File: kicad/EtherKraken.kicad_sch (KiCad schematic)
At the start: 4 parts

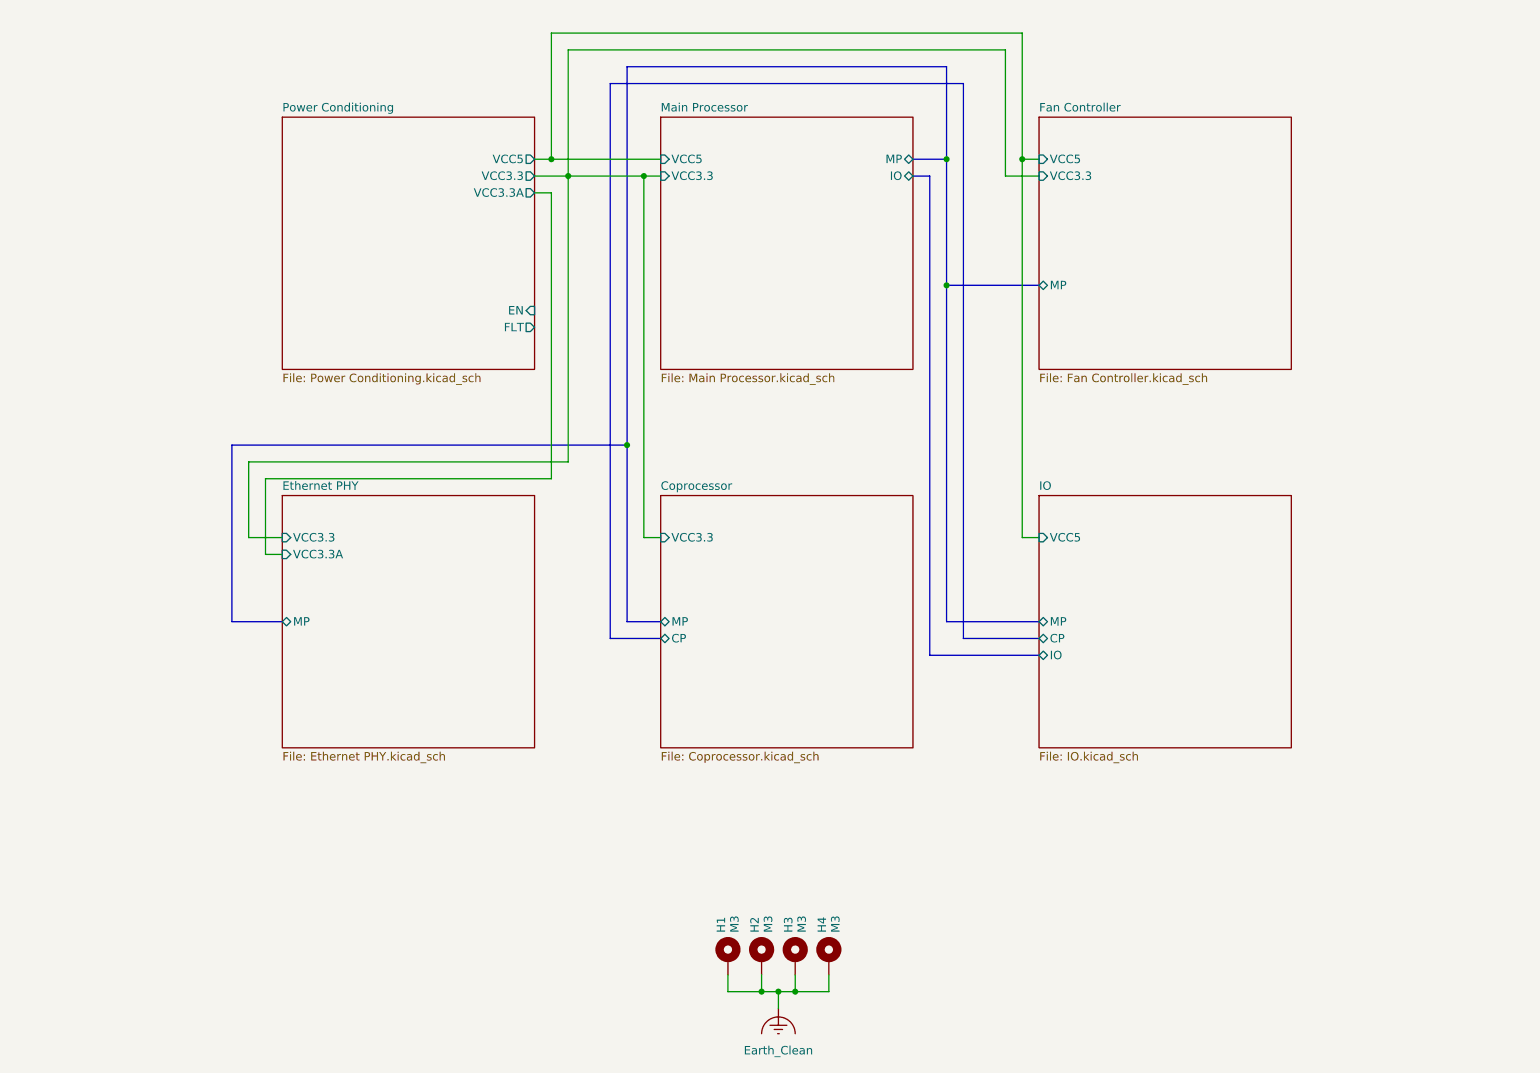
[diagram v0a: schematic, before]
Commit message: Add main bus to root schematic, use bus labels for exporting IO and CPIO busses
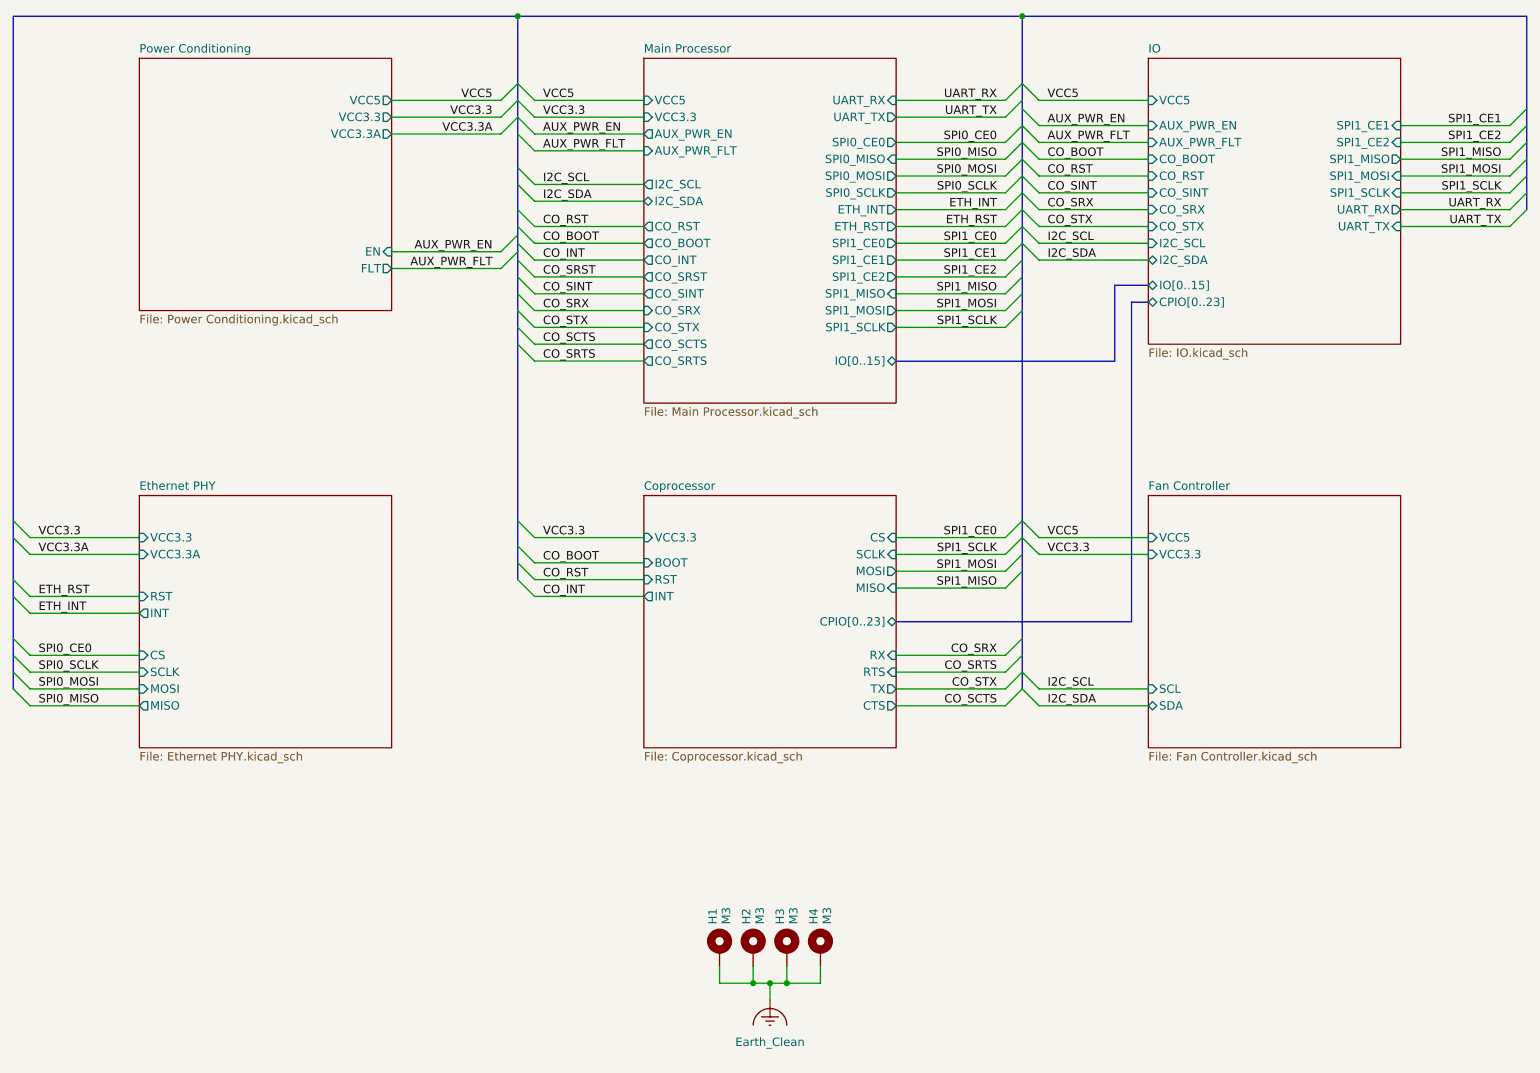
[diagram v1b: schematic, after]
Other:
- sheet Coprocessor ports: added BOOT, CPIO[0..23], CS, CTS, INT, MISO, MOSI, RST, RTS, RX, SCLK, TX; removed CP, MP
- sheet Ethernet PHY ports: added CS, INT, MISO, MOSI, RST, SCLK; removed MP
- sheet Fan Controller ports: added SCL, SDA; removed MP
- sheet IO ports: added AUX_PWR_EN, AUX_PWR_FLT, CO_BOOT, CO_RST, CO_SINT, CO_SRX, CO_STX, CPIO[0..23], I2C_SCL, I2C_SDA, IO[0..15], SPI1_CE1, SPI1_CE2, SPI1_MISO, SPI1_MOSI, SPI1_SCLK, UART_RX, UART_TX; removed CP, IO, MP
- sheet Main Processor ports: added AUX_PWR_EN, AUX_PWR_FLT, CO_BOOT, CO_INT, CO_RST, CO_SCTS, CO_SINT, CO_SRST, CO_SRTS, CO_SRX, CO_STX, ETH_INT, ETH_RST, I2C_SCL, I2C_SDA, IO[0..15], SPI0_CE0, SPI0_MISO, SPI0_MOSI, SPI0_SCLK, SPI1_CE0, SPI1_CE1, SPI1_CE2, SPI1_MISO, SPI1_MOSI, SPI1_SCLK, UART_RX, UART_TX; removed IO, MP
- moved on the sheet: H1, H2, H3, H4
